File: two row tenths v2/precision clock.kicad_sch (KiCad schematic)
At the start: 59 parts, among them P1 USB_C_Plug_USB2.0, P2 USB_C_Plug_USB2.0, Q1 MMBT3904

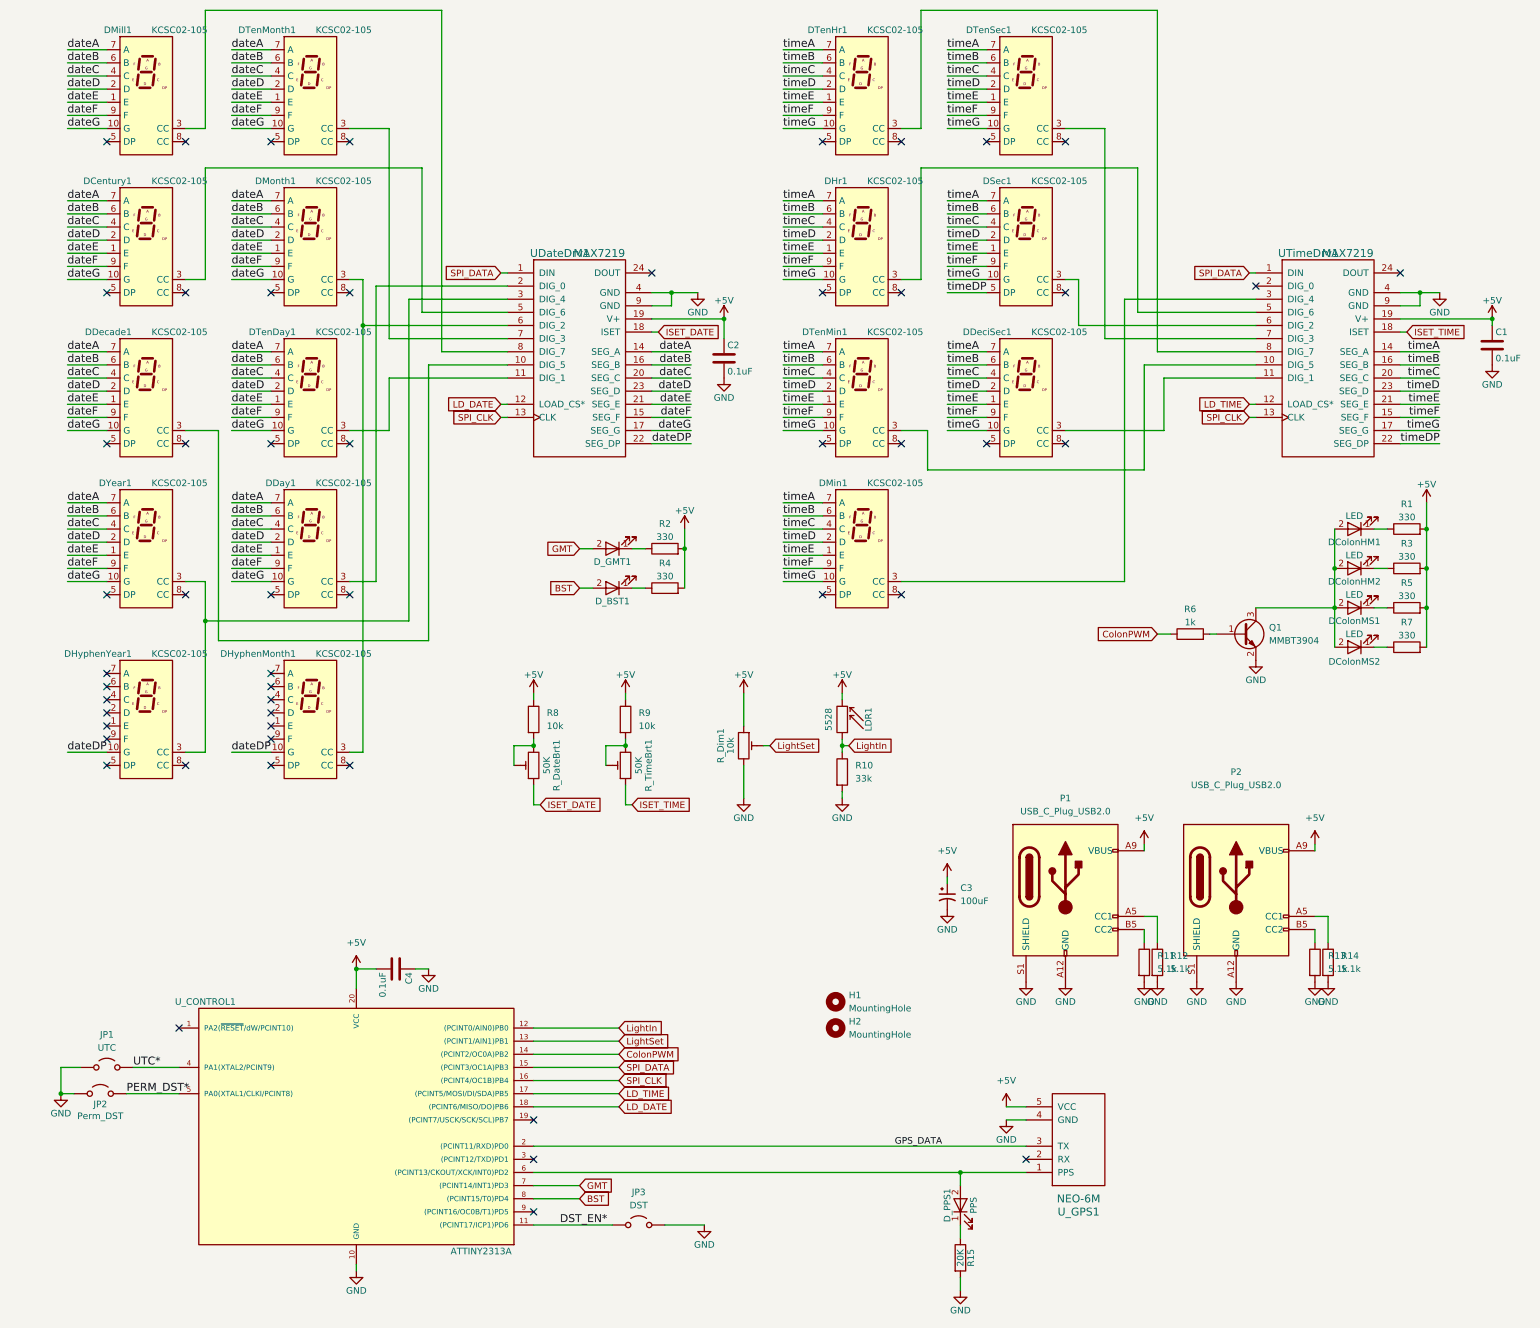
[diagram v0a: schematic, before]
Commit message: Add 74AHCT125 as PWM driver
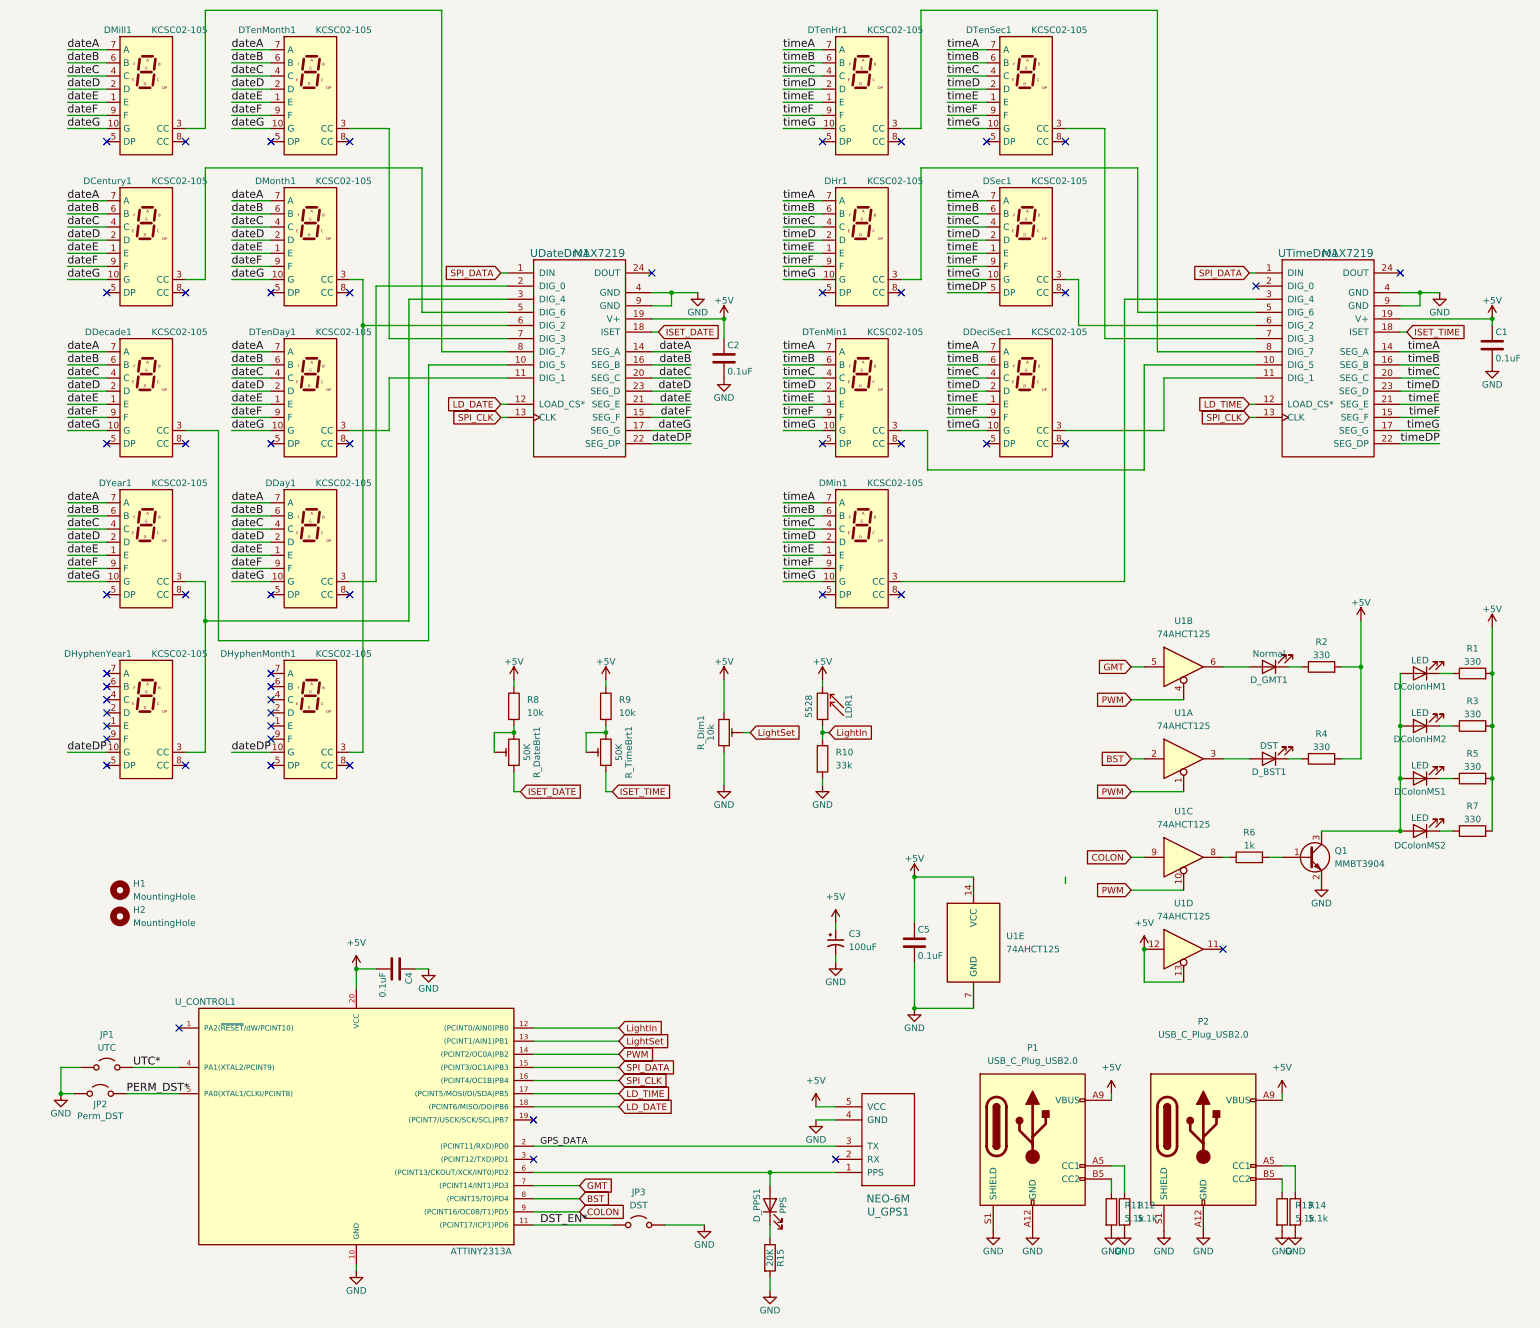
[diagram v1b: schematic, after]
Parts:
- added C5: 0.1uF, Capacitor_SMD:C_1206_3216Metric, symbol Device:C
- added U1: 74AHCT125, Package_SO:SOIC-14_3.9x8.7mm_P1.27mm, symbol 74xx:74AHCT125
- C1, C2, C4: symbol precision-clock-rescue:C -> Device:C
- C3: footprint Capacitor_THT:CP_Radial_D5.0mm_P2.50mm -> Capacitor_THT:CP_Radial_D6.3mm_P2.50mm
- DCentury1, DDay1, DDecade1, DDeciSec1, DHr1, DHyphenMonth1, DHyphenYear1, DMill1, DMin1, DMonth1, DSec1, DTenDay1, DTenHr1, DTenMin1, DTenMonth1, DTenSec1, DYear1: symbol precision-clock-rescue:KCSC02-105 -> precision clock:KCSC02-105-precision-clock
- DColonHM1, DColonHM2, DColonMS1, DColonMS2, D_PPS1: symbol precision-clock-rescue:LED -> Device:LED
- D_BST1: value ~ -> DST; symbol precision-clock-rescue:LED -> Device:LED
- D_GMT1: value ~ -> Normal; symbol precision-clock-rescue:LED -> Device:LED
- LDR1: symbol precision-clock-rescue:LDR03 -> precision clock-rescue:LDR03-precision-clock-rescue
- R15: symbol precision-clock-rescue:R -> precision clock-rescue:R-precision-clock-rescue
- R_DateBrt1, R_Dim1, R_TimeBrt1: symbol precision-clock-rescue:POT_TRIM -> precision clock-rescue:POT_TRIM-precision-clock-rescue
- UDateDrv1, UTimeDrv1: symbol precision-clock-rescue:MAX7219 -> precision clock-rescue:MAX7219-precision-clock-rescue
- U_CONTROL1: symbol precision-clock-rescue:ATTINY2313A-PU -> precision clock:ATTINY2313A-PU-precision-clock
- U_GPS1: symbol precision-clock-rescue:NEO6MV2 -> precision clock-rescue:NEO6MV2-precision-clock-rescue
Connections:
- net +5V: now also C5.1, U1.12, U1.13, U1.14 (VCC)
- net BST: now also U1.2; no longer D_BST1.2 (A)
- net GMT: now also U1.5; no longer D_GMT1.2 (A)
- net GND: now also C5.2, U1.7 (GND)
- net COLON: now reaches U_CONTROL1.9 ((PCINT16/OC0B/T1)PD5)
- net COLON: now also U1.9
- net ColonPWM: no longer names the net of R6.1
- net ColonPWM: now also U1.8; no longer U_CONTROL1.14 ((PCINT2/OC0A)PB2)
- new net: D_GMT1.2 (A), U1.6
- new net: D_BST1.2 (A), U1.3
- new net PWM: U1.1, U1.10, U1.4, U_CONTROL1.14 ((PCINT2/OC0A)PB2)
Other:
- moved on the sheet: C3, H1, H2, LDR1, P1, P2, Q1, R1, R10, R11, R12, R13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

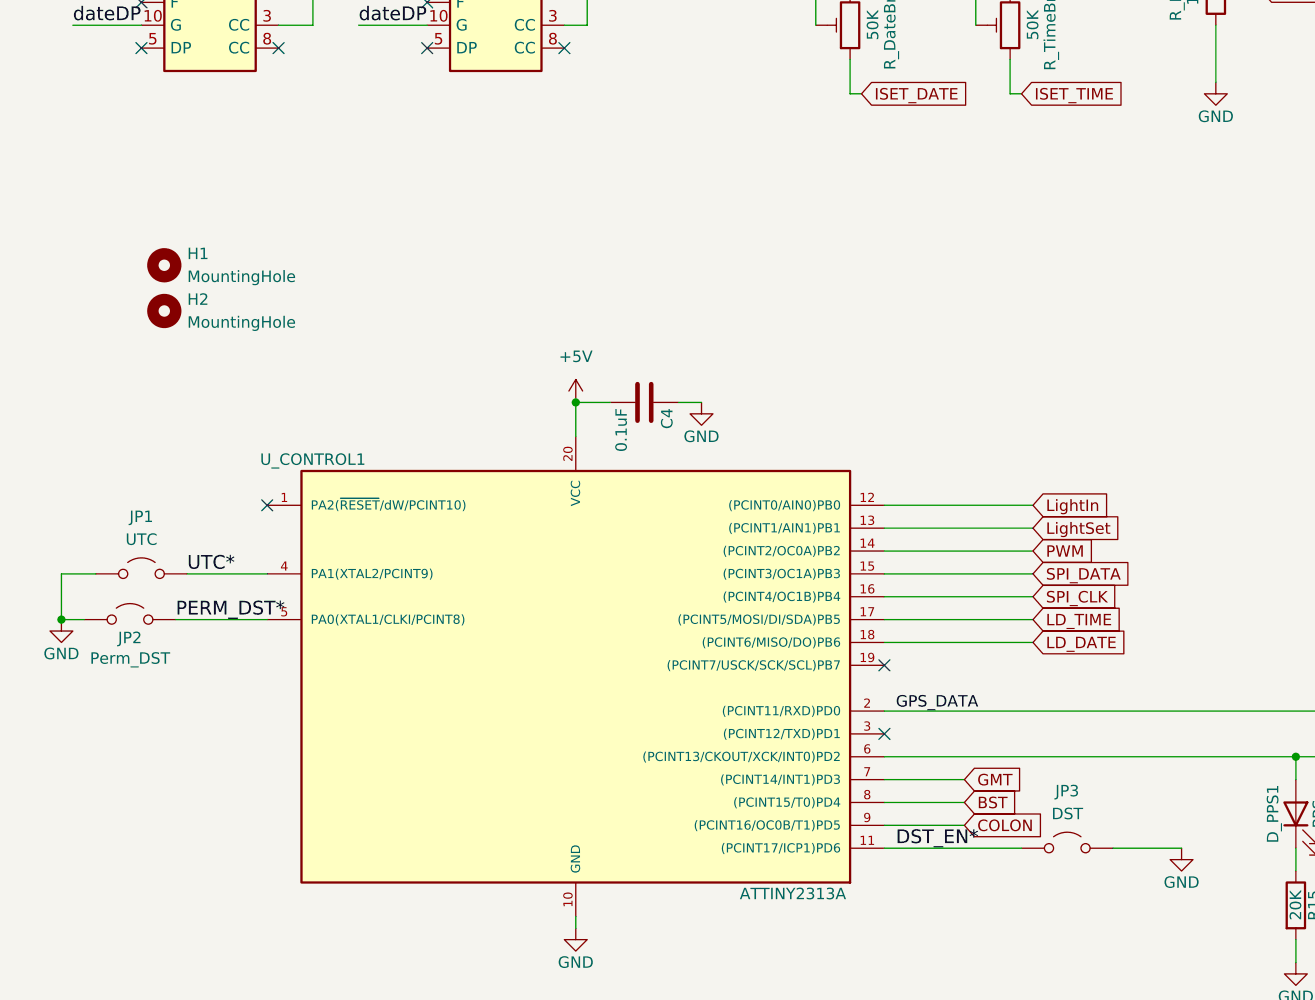
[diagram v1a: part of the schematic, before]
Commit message: Add optional crystal
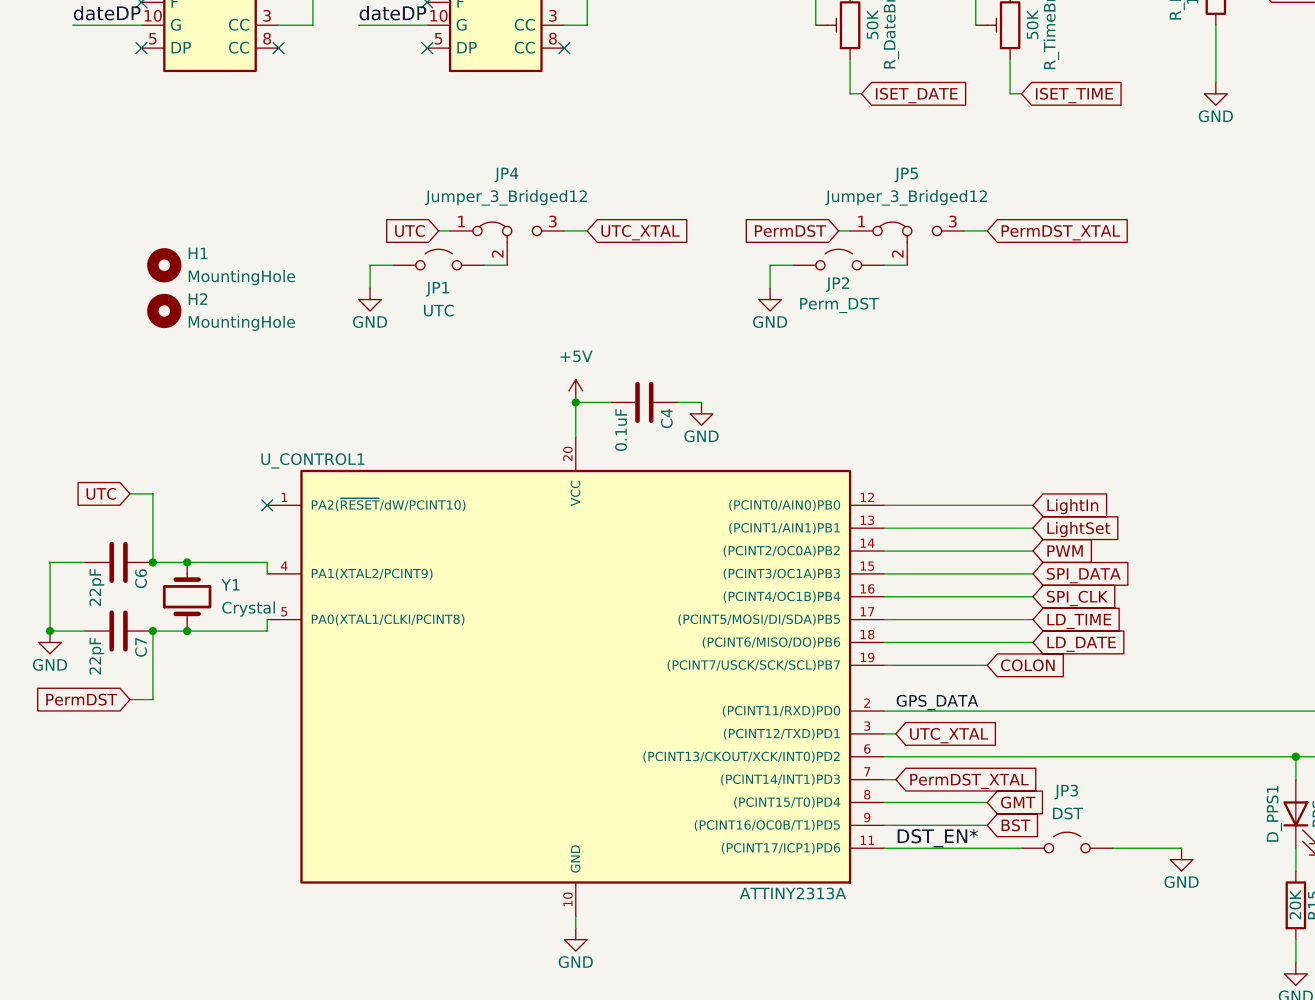
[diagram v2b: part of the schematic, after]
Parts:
- added C6, C7: 22pF, Capacitor_SMD:C_1206_3216Metric, symbol Device:C
- added JP4, JP5: Jumper_3_Bridged12, Jumper:SolderJumper-3_P1.3mm_Bridged2Bar12_Pad1.0x1.5mm, symbol Jumper:Jumper_3_Bridged12
- added Y1: Crystal, Crystal:Crystal_SMD_HC49-SD, symbol Device:Crystal
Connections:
- net BST: now also U_CONTROL1.9 ((PCINT16/OC0B/T1)PD5); no longer U_CONTROL1.8 ((PCINT15/T0)PD4)
- net COLON: now also U_CONTROL1.19 ((PCINT7/USCK/SCK/SCL)PB7); no longer U_CONTROL1.9 ((PCINT16/OC0B/T1)PD5)
- net GMT: now also U_CONTROL1.8 ((PCINT15/T0)PD4); no longer U_CONTROL1.7 ((PCINT14/INT1)PD3)
- net GND: now also C6.2, C7.2
- net UTC_XTAL: now reaches U_CONTROL1.3 ((PCINT12/TXD)PD1)
- net UTC_XTAL: now also JP4.3 (B)
- net PERM_DST*: no longer names the net of JP2.1 (A)
- net PERM_DST*: now also JP5.2 (C); no longer U_CONTROL1.5 (PA0(XTAL1/CLKI/PCINT8))
- net UTC*: no longer names the net of JP1.1 (A)
- net UTC*: now also JP4.2 (C); no longer U_CONTROL1.4 (PA1(XTAL2/PCINT9))
- new net PermDST: C7.1, JP5.1 (A), U_CONTROL1.5 (PA0(XTAL1/CLKI/PCINT8)), Y1.1
- new net PermDST_XTAL: JP5.3 (B), U_CONTROL1.7 ((PCINT14/INT1)PD3)
- new net UTC: C6.1, JP4.1 (A), U_CONTROL1.4 (PA1(XTAL2/PCINT9)), Y1.2
- no-connect marks 53 -> 51
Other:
- moved on the sheet: JP1, JP2
